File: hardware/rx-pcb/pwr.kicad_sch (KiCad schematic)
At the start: 0 parts

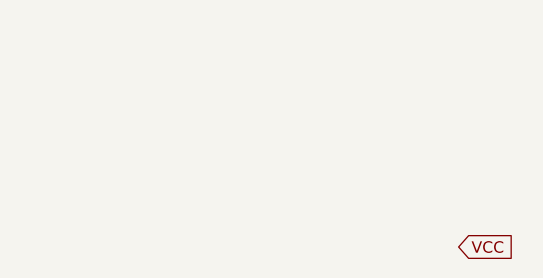
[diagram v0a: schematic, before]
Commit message: finished V1 of receiver PCB. No power electronics yet.
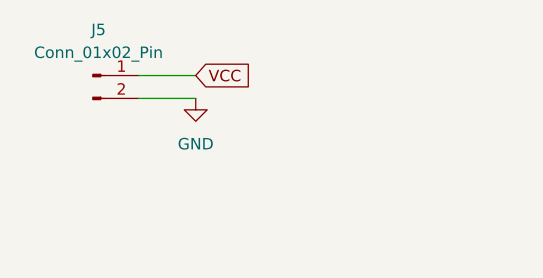
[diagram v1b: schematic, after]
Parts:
- added J5: Conn_01x02_Pin, Connector_PinHeader_2.54mm:PinHeader_1x02_P2.54mm_Vertical, symbol Connector:Conn_01x02_Pin
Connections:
- net VCC: now also J5.1 (Pin_1)
- new net GND: J5.2 (Pin_2)
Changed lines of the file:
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@@
 	(generator_version "9.0")
 	(paper "A4")
+	(wire
+		(pts
+			(xy 39.37 36.83) (xy 45.72 36.83)
+		)
+		(stroke
+			(width 0)
+			(type default)
+		)
+	)
+	(wire
+		(pts
+			(xy 39.37 39.37) (xy 45.72 39.37)
+		)
+		(stroke
+			(width 0)
+			(type default)
+		)
+	)
 	(global_label "VCC"
 		(shape input)
-		(at 74.93 55.88 0)
+		(at 45.72 36.83 0)
 		(fields_autoplaced yes)
 		(effects
@@
 		)
 		(property "Intersheetrefs" "${INTERSHEET_REFS}"
-			(at 81.5438 55.88 0)
+			(at 52.3338 36.83 0)
 			(effects
 				(font
@@
 			)
 		)
+	)
+	(symbol
+		(lib_id "rx-parts:GND")
+		(at 45.72 39.37 0)
+		(unit 1)
+		(exclude_from_sim no)
+		(in_bom yes)
+		(on_board yes)
+		(dnp no)
+		(fields_autoplaced yes)
+		(property "Reference" "#PWR021"
+			(at 45.72 45.72 0)
+			(effects
+				(font
+					(size 1.27 1.27)
+				)
+				(hide yes)
+			)
+		)
+		(property "Value" "GND"
+			(at 45.72 44.45 0)
+			(effects
+				(font
+					(size 1.27 1.27)
+				)
+			)
+		)
+		(property "Footprint" ""
+			(at 45.72 39.37 0)
+			(effects
+				(font
+					(size 1.27 1.27)
+				)
+				(hide yes)
+			)
+		)
+		(property "Datasheet" ""
+			(at 45.72 39.37 0)
+			(effects
+				(font
+					(size 1.27 1.27)
+				)
+				(hide yes)
+			)
+		)
+		(property "Description" "Power symbol creates a global label with name \"GND\" , ground"
+			(at 45.72 39.37 0)
+			(effects
+				(font
+					(size 1.27 1.27)
+				)
+				(hide yes)
+			)
+		)
+		(pin "1"
+		)
+		(instances
+			(project ""
+				(path "/9df8ddb8-545e-44cf-b4e7-941b19ec42ab/8aa431ec-54c0-4ed8-905f-3367f0528530"
+					(reference "#PWR021")
+					(unit 1)
+				)
+			)
+		)
+	)
+	(symbol
+		(lib_id "Connector:Conn_01x02_Pin")
+		(at 34.29 36.83 0)
+		(unit 1)
+		(exclude_from_sim no)
+		(in_bom yes)
+		(on_board yes)
+		(dnp no)
+		(fields_autoplaced yes)
+		(property "Reference" "J5"
+			(at 34.925 31.75 0)
+			(effects
+				(font
+					(size 1.27 1.27)
+				)
+			)
+		)
+		(property "Value" "Conn_01x02_Pin"
+			(at 34.925 34.29 0)
+			(effects
+				(font
+					(size 1.27 1.27)
+				)
+			)
+		)
+		(property "Footprint" "Connector_PinHeader_2.54mm:PinHeader_1x02_P2.54mm_Vertical"
+			(at 34.29 36.83 0)
+			(effects
+				(font
+					(size 1.27 1.27)
+				)
+				(hide yes)
+			)
+		)
+		(property "Datasheet" "~"
+			(at 34.29 36.83 0)
+			(effects
+				(font
+					(size 1.27 1.27)
+				)
+				(hide yes)
+			)
+		)
+		(property "Description" "Generic connector, single row, 01x02, script generated"
+			(at 34.29 36.83 0)
+			(effects
+				(font
+					(size 1.27 1.27)
+				)
+				(hide yes)
+			)
+		)
+		(pin "2"
+		)
+		(pin "1"
+		)
+		(instances
+			(project ""
+				(path "/9df8ddb8-545e-44cf-b4e7-941b19ec42ab/8aa431ec-54c0-4ed8-905f-3367f0528530"
+					(reference "J5")
+					(unit 1)
+				)
+			)
+		)
